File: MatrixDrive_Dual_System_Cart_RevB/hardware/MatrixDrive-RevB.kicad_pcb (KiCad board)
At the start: 2 copper layers, 100 x 65 mm, 23 parts, among them J1 MEGA_DRIVE_EDGE_VERIFY_ORIENT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, J2 USB-C, J4 CPLD JTAG, SW1 PROGRAM, SW2 MD / SMS, SW3 SMS PAUSE, U1 RP2350B QFN80, U10 STAGING SPI, U11 3V3 LDO, U13 ATF1508ASV CPLD, U14 CTRL2 XCVR, U15-U16 DATA CONTROL, U17 32KiB SMS FRAM, U2 S29GL032N TSOP48, U3 ADDR XCVR 0-7, U4 ADDR XCVR 8-15, U5 ADDR/CTRL XCVR, U6 LOW DATA BIDI, U7 HIGH DATA OUT, U9 BOOT QSPI, Y1 12MHz

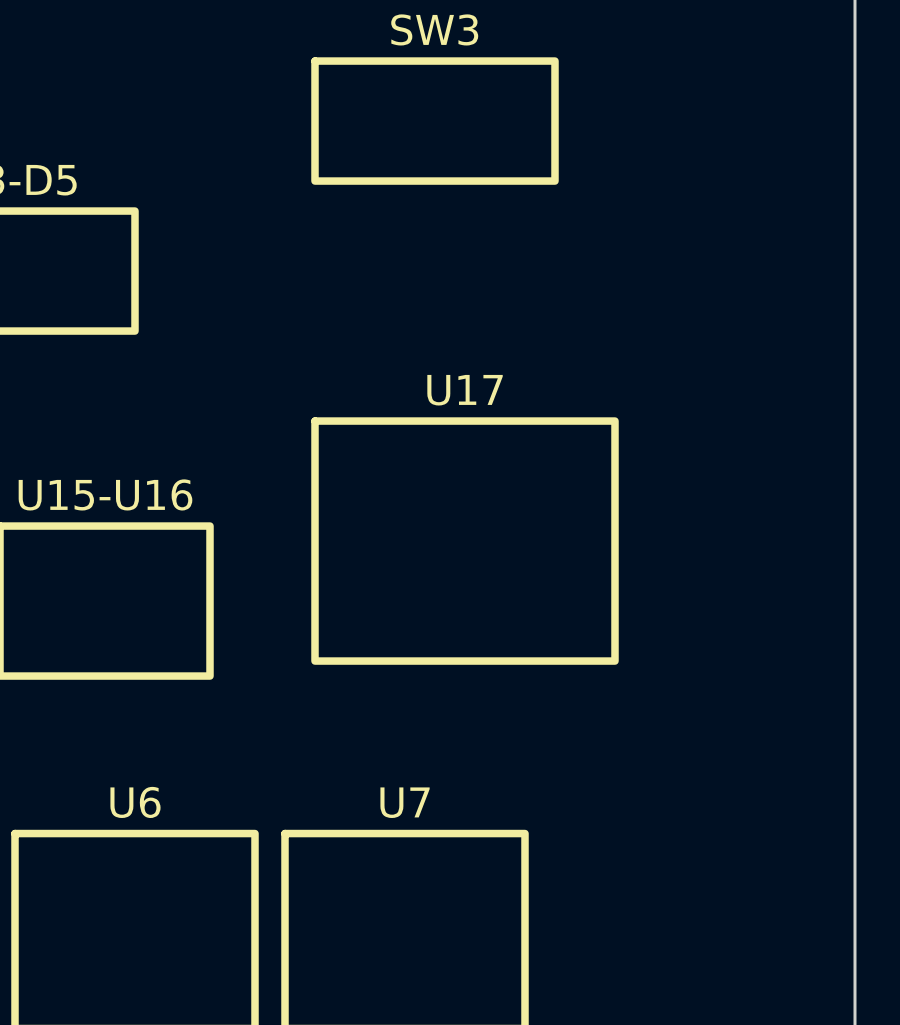
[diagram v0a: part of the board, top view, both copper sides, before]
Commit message: Add Codemasters SMS mapper and 64 KiB FRAM
Adds SW4 Sega/Codemasters selection, exact Codemasters banking and RAM decode, two-chip 64 KiB FRAM, updated hardware documentation, RTL tests, and rebuilt RP2350B firmware package.
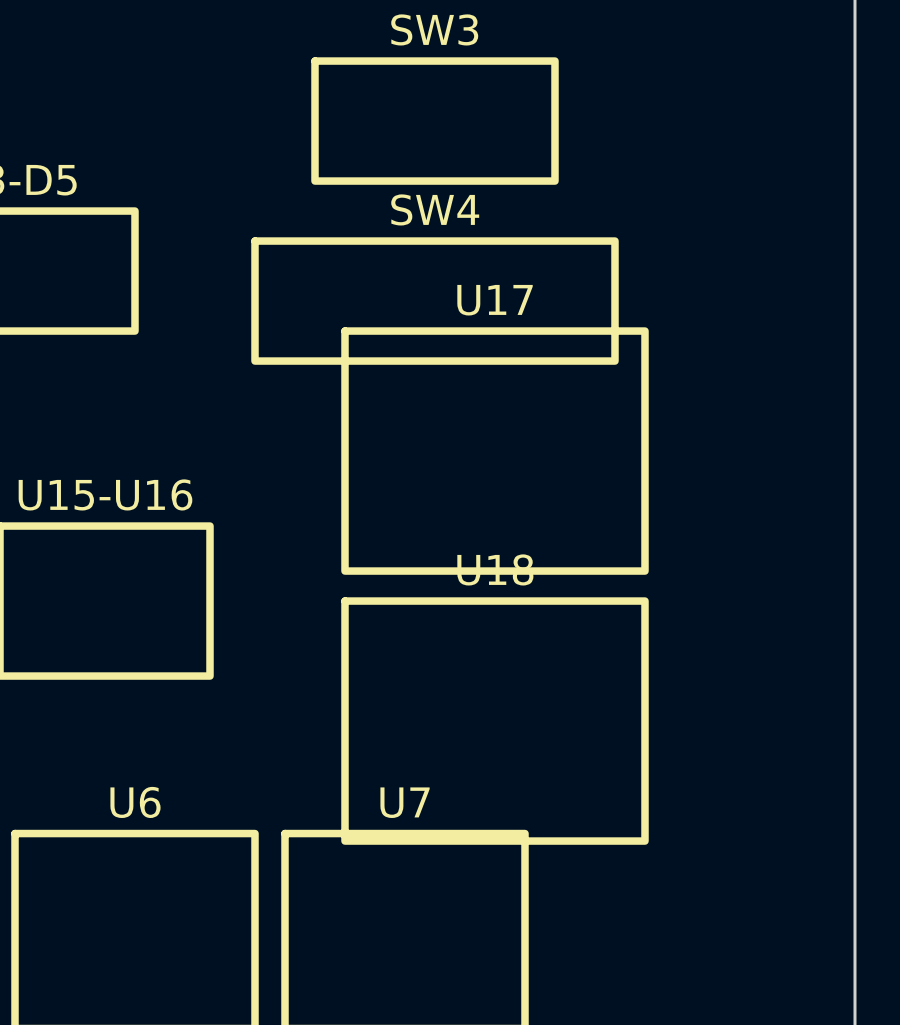
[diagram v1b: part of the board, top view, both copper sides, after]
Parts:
- added SW4: SEGA / CODEMASTERS, MatrixDrive:PLACEMENT_SW4, F.Cu at (86.0, 20.0)
- added U18: 32KiB FRAM HIGH, MatrixDrive:PLACEMENT_U18, F.Cu at (88.0, 34.0)
- U17: value 32KiB SMS FRAM -> 32KiB FRAM LOW
- moved U17 3.16 mm to (88.0, 25.0)
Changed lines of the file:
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@@
       (effects (font (size 0.8 0.8) (thickness 0.12))))
   )
-  (footprint "MatrixDrive:PLACEMENT_U17" (layer "F.Cu") (at 87.00 28.00)
+  (footprint "MatrixDrive:PLACEMENT_U17" (layer "F.Cu") (at 88.00 25.00)
     (attr board_only exclude_from_pos_files exclude_from_bom)
     (fp_rect (start -5.00 -4.00) (end 5.00 4.00)
@@
     (fp_text reference "U17" (at 0 -5.00) (layer "F.SilkS")
       (effects (font (size 1 1) (thickness 0.15))))
-    (fp_text value "32KiB SMS FRAM" (at 0 0) (layer "F.Fab")
+    (fp_text value "32KiB FRAM LOW" (at 0 0) (layer "F.Fab")
+      (effects (font (size 0.8 0.8) (thickness 0.12))))
+  )
+  (footprint "MatrixDrive:PLACEMENT_U18" (layer "F.Cu") (at 88.00 34.00)
+    (attr board_only exclude_from_pos_files exclude_from_bom)
+    (fp_rect (start -5.00 -4.00) (end 5.00 4.00)
+      (stroke (width 0.25) (type default)) (fill none) (layer "F.SilkS"))
+    (fp_text reference "U18" (at 0 -5.00) (layer "F.SilkS")
+      (effects (font (size 1 1) (thickness 0.15))))
+    (fp_text value "32KiB FRAM HIGH" (at 0 0) (layer "F.Fab")
       (effects (font (size 0.8 0.8) (thickness 0.12))))
   )
@@
       (effects (font (size 0.8 0.8) (thickness 0.12))))
   )
+  (footprint "MatrixDrive:PLACEMENT_SW4" (layer "F.Cu") (at 86.00 20.00)
+    (attr board_only exclude_from_pos_files exclude_from_bom)
+    (fp_rect (start -6.00 -2.00) (end 6.00 2.00)
+      (stroke (width 0.25) (type default)) (fill none) (layer "F.SilkS"))
+    (fp_text reference "SW4" (at 0 -3.00) (layer "F.SilkS")
+      (effects (font (size 1 1) (thickness 0.15))))
+    (fp_text value "SEGA / CODEMASTERS" (at 0 0) (layer "F.Fab")
+      (effects (font (size 0.8 0.8) (thickness 0.12))))
+  )

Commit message: Regenerate lock-on PCB template and package [skip ci]
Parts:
- added U19: MD HIGH DISABLE XCVR, MatrixDrive:PLACEMENT_U19, F.Cu at (75.0, 24.0)
- added U20: SONIC 3 SAVE FRAM, MatrixDrive:PLACEMENT_U20, F.Cu at (88.0, 51.0)
- SW4: value SEGA / CODEMASTERS -> SEGA-LINEAR / CODIES-S3 SAVE
- U15-U16: value DATA CONTROL -> DATA CONTROL ORS
- U17: value 32KiB FRAM LOW -> 32KiB SMS FRAM LOW
- U18: value 32KiB FRAM HIGH -> 32KiB SMS FRAM HIGH
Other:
- board text added: "MATRIXDRIVE REV B DUAL-SYSTEM + LOCK-ON — PLACEMENT ONLY"
- board text added: "STANDARD MD EDGE / S&K UPPER-SLOT PROFILE — VERIFY SHELL"
- board text removed: "B1/A1 AT LEFT IN THIS VIEW — VERIFY AGAINST DONOR"
- board text removed: "MATRIXDRIVE REV B DUAL-SYSTEM — PLACEMENT ONLY"
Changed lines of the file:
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@@
   (setup (pad_to_mask_clearance 0))
   (gr_rect (start 0 0) (end 100 65) (stroke (width 0.10) (type default)) (fill none) (layer "Edge.Cuts"))
-  (gr_text "MATRIXDRIVE REV B DUAL-SYSTEM — PLACEMENT ONLY" (at 50.00 3.00) (layer "F.SilkS")
+  (gr_text "MATRIXDRIVE REV B DUAL-SYSTEM + LOCK-ON — PLACEMENT ONLY" (at 50.00 3.00) (layer "F.SilkS")
     (effects (font (size 1.20 1.20) (thickness 0.20)))
   )
@@
     (fp_text reference "U15-U16" (at 0 -3.50) (layer "F.SilkS")
       (effects (font (size 1 1) (thickness 0.15))))
-    (fp_text value "DATA CONTROL" (at 0 0) (layer "F.Fab")
+    (fp_text value "DATA CONTROL ORS" (at 0 0) (layer "F.Fab")
       (effects (font (size 0.8 0.8) (thickness 0.12))))
   )
@@
     (fp_text reference "U17" (at 0 -5.00) (layer "F.SilkS")
       (effects (font (size 1 1) (thickness 0.15))))
-    (fp_text value "32KiB FRAM LOW" (at 0 0) (layer "F.Fab")
+    (fp_text value "32KiB SMS FRAM LOW" (at 0 0) (layer "F.Fab")
       (effects (font (size 0.8 0.8) (thickness 0.12))))
   )
@@
     (fp_text reference "U18" (at 0 -5.00) (layer "F.SilkS")
       (effects (font (size 1 1) (thickness 0.15))))
-    (fp_text value "32KiB FRAM HIGH" (at 0 0) (layer "F.Fab")
+    (fp_text value "32KiB SMS FRAM HIGH" (at 0 0) (layer "F.Fab")
+      (effects (font (size 0.8 0.8) (thickness 0.12))))
+  )
+  (footprint "MatrixDrive:PLACEMENT_U19" (layer "F.Cu") (at 75.00 24.00)
+    (attr board_only exclude_from_pos_files exclude_from_bom)
+    (fp_rect (start -3.00 -2.00) (end 3.00 2.00)
+      (stroke (width 0.25) (type default)) (fill none) (layer "F.SilkS"))
+    (fp_text reference "U19" (at 0 -3.00) (layer "F.SilkS")
+      (effects (font (size 1 1) (thickness 0.15))))
+    (fp_text value "MD HIGH DISABLE XCVR" (at 0 0) (layer "F.Fab")
+      (effects (font (size 0.8 0.8) (thickness 0.12))))
+  )
+  (footprint "MatrixDrive:PLACEMENT_U20" (layer "F.Cu") (at 88.00 51.00)
+    (attr board_only exclude_from_pos_files exclude_from_bom)
+    (fp_rect (start -5.00 -4.00) (end 5.00 4.00)
+      (stroke (width 0.25) (type default)) (fill none) (layer "F.SilkS"))
+    (fp_text reference "U20" (at 0 -5.00) (layer "F.SilkS")
+      (effects (font (size 1 1) (thickness 0.15))))
+    (fp_text value "SONIC 3 SAVE FRAM" (at 0 0) (layer "F.Fab")
       (effects (font (size 0.8 0.8) (thickness 0.12))))
   )
@@
   (footprint "MatrixDrive:PLACEMENT_SW4" (layer "F.Cu") (at 86.00 20.00)
     (attr board_only exclude_from_pos_files exclude_from_bom)
-    (fp_rect (start -6.00 -2.00) (end 6.00 2.00)
+    (fp_rect (start -8.00 -2.00) (end 8.00 2.00)
       (stroke (width 0.25) (type default)) (fill none) (layer "F.SilkS"))
     (fp_text reference "SW4" (at 0 -3.00) (layer "F.SilkS")
       (effects (font (size 1 1) (thickness 0.15))))
-    (fp_text value "SEGA / CODEMASTERS" (at 0 0) (layer "F.Fab")
+    (fp_text value "SEGA-LINEAR / CODIES-S3 SAVE" (at 0 0) (layer "F.Fab")
       (effects (font (size 0.8 0.8) (thickness 0.12))))
   )
@@
       (effects (font (size 0.8 0.8) (thickness 0.12))))
   )
-  (gr_text "B1/A1 AT LEFT IN THIS VIEW — VERIFY AGAINST DONOR" (at 50.00 56.00) (layer "F.SilkS")
+  (gr_text "STANDARD MD EDGE / S&K UPPER-SLOT PROFILE — VERIFY SHELL" (at 50.00 56.00) (layer "F.SilkS")
     (effects (font (size 1.20 1.20) (thickness 0.20)))
   )

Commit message: Add real 32X cartridge ROM support
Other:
- board text added: "STANDARD MD / 32X EDGE / S&K UPPER-SLOT — VERIFY SHELL"
- board text removed: "STANDARD MD EDGE / S&K UPPER-SLOT PROFILE — VERIFY SHELL"
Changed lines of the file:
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@@
       (effects (font (size 0.8 0.8) (thickness 0.12))))
   )
-  (gr_text "STANDARD MD EDGE / S&K UPPER-SLOT PROFILE — VERIFY SHELL" (at 50.00 56.00) (layer "F.SilkS")
+  (gr_text "STANDARD MD / 32X EDGE / S&K UPPER-SLOT — VERIFY SHELL" (at 50.00 56.00) (layer "F.SilkS")
     (effects (font (size 1.20 1.20) (thickness 0.20)))
   )

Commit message: Add complete MatrixDrive KiCad project
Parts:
- removed D3-D5: STATUS LEDS, MatrixDrive:PLACEMENT_D3-D5
- removed U15-U16: DATA CONTROL ORS, MatrixDrive:PLACEMENT_U15-U16
- added C1: 100nF, MatrixDrive:0603, F.Cu at (58.9, 22.4)
- added C10: 100nF, MatrixDrive:0603, F.Cu at (37.4, 26.5)
- added C11: 100nF, MatrixDrive:0603, F.Cu at (41.7, 26.5)
- added C12: 100nF, MatrixDrive:0603, F.Cu at (46.0, 26.5)
- added C13: 100nF, MatrixDrive:0603, F.Cu at (50.3, 26.5)
- added C14: 100nF, MatrixDrive:0603, F.Cu at (54.6, 26.5)
- added C15: 100nF, MatrixDrive:0603, F.Cu at (58.9, 26.5)
- added C16: 100nF, MatrixDrive:0603, F.Cu at (63.2, 26.5)
- added C17: 100nF, MatrixDrive:0603, F.Cu at (67.5, 26.5)
- added C18: 100nF, MatrixDrive:0603, F.Cu at (93.3, 26.5)
- added C19: 1uF, MatrixDrive:0603, F.Cu at (3.00, 30.6)
- added C2: 100nF, MatrixDrive:0603, F.Cu at (63.2, 22.4)
- added C20: 1uF, MatrixDrive:0603, F.Cu at (7.30, 30.6)
- added C21: 1uF, MatrixDrive:0603, F.Cu at (20.2, 30.6)
- added C22: 1uF, MatrixDrive:0603, F.Cu at (33.1, 30.6)
- added C23: 10uF, MatrixDrive:0805, F.Cu at (37.4, 30.6)
- added C24: 10uF, MatrixDrive:0805, F.Cu at (41.7, 30.6)
- added C25: 15pF, MatrixDrive:0402, F.Cu at (46.0, 30.6)
- added C26: 15pF, MatrixDrive:0402, F.Cu at (50.3, 30.6)
- added C27: 4.7uF, MatrixDrive:0603, F.Cu at (54.6, 30.6)
- added C28: TBD_REF, MatrixDrive:0402, F.Cu at (58.9, 30.6)
- added C29: TBD_REF, MatrixDrive:0402, F.Cu at (63.2, 30.6)
- added C3: 100nF, MatrixDrive:0603, F.Cu at (67.5, 22.4)
- added C30: TBD_REF, MatrixDrive:0402, F.Cu at (67.5, 30.6)
- added C31: TBD_REF, MatrixDrive:0402, F.Cu at (93.3, 30.6)
- added C32: TBD_REF, MatrixDrive:0402, F.Cu at (3.00, 34.7)
- added C33: TBD_REF, MatrixDrive:0402, F.Cu at (7.30, 34.7)
- added C34: 100nF, MatrixDrive:0603, F.Cu at (20.2, 34.7)
- added C35: 100nF, MatrixDrive:0603, F.Cu at (33.1, 34.7)
- added C36: 100nF, MatrixDrive:0603, F.Cu at (37.4, 34.7)
- added C4: 100nF, MatrixDrive:0603, F.Cu at (80.4, 22.4)
- added C5: 100nF, MatrixDrive:0603, F.Cu at (93.3, 22.4)
- added C6: 100nF, MatrixDrive:0603, F.Cu at (3.00, 26.5)
- added C7: 100nF, MatrixDrive:0603, F.Cu at (7.30, 26.5)
- added C8: 100nF, MatrixDrive:0603, F.Cu at (20.2, 26.5)
- added C9: 100nF, MatrixDrive:0603, F.Cu at (33.1, 26.5)
- added D1: PMEG2010AEB, MatrixDrive:SOD_523, F.Cu at (15.9, 6.00)
- added D2: PMEG2010AEB, MatrixDrive:SOD_523, F.Cu at (28.8, 6.00)
- added D3: GREEN_LED, MatrixDrive:0603_LED, F.Cu at (33.1, 6.00)
- added D4: AMBER_LED, MatrixDrive:0603_LED, F.Cu at (37.4, 6.00)
- added D5: RED_LED, MatrixDrive:0603_LED, F.Cu at (41.7, 6.00)
- added F1: MF-MSMF020-2, MatrixDrive:1812, F.Cu at (3.00, 6.00)
- added J3: SWD_UART_2x5 DNP, MatrixDrive:HDR_2x5_1_27, F.Cu at (66.0, 5.00)
- added Q1: 2N7002, MatrixDrive:SOT_23, F.Cu at (80.4, 6.00)
- added Q2: 2N7002, MatrixDrive:SOT_23, F.Cu at (93.3, 6.00)
- added Q3: 2N7002, MatrixDrive:SOT_23, F.Cu at (3.00, 10.1)
- added Q4: 2N7002, MatrixDrive:SOT_23, F.Cu at (7.30, 10.1)
- added R1: 5.1k, MatrixDrive:0603, F.Cu at (33.1, 10.1)
- added R10: 1k, MatrixDrive:0603, F.Cu at (15.9, 14.2)
- added R11: 1k, MatrixDrive:0603, F.Cu at (20.2, 14.2)
- added R12: 10k, MatrixDrive:0603, F.Cu at (24.5, 14.2)
- added R13: 0R, MatrixDrive:0603, F.Cu at (28.8, 14.2)
- added R14: 100k, MatrixDrive:0603, F.Cu at (33.1, 14.2)
- added R15: 10k DNP, MatrixDrive:0603, F.Cu at (54.6, 14.2)
- added R16: 10k DNP, MatrixDrive:0603, F.Cu at (67.5, 14.2)
- added R17: 10k DNP, MatrixDrive:0603, F.Cu at (71.8, 14.2)
- added R18: 10k DNP, MatrixDrive:0603, F.Cu at (76.1, 14.2)
- added R19: 10k, MatrixDrive:0603, F.Cu at (80.4, 14.2)
- added R2: 5.1k, MatrixDrive:0603, F.Cu at (67.5, 10.1)
- added R20: 10k, MatrixDrive:0603, F.Cu at (93.3, 14.2)
- added R21: 10k, MatrixDrive:0603, F.Cu at (3.00, 18.3)
- added R22: 10k, MatrixDrive:0603, F.Cu at (7.30, 18.3)
- added R23: 10k, MatrixDrive:0603, F.Cu at (11.6, 18.3)
- added R24: 33R, MatrixDrive:0603, F.Cu at (15.9, 18.3)
- added R25: 10k, MatrixDrive:0603, F.Cu at (20.2, 18.3)
- added R26: 10k, MatrixDrive:0603, F.Cu at (33.1, 18.3)
- added R27: 10k, MatrixDrive:0603, F.Cu at (37.4, 18.3)
- added R28: 1k, MatrixDrive:0603, F.Cu at (41.7, 18.3)
- added R29: 100k, MatrixDrive:0603, F.Cu at (54.6, 18.3)
- added R3: 27R, MatrixDrive:0603, F.Cu at (71.8, 10.1)
- added R30: 100k, MatrixDrive:0603, F.Cu at (58.9, 18.3)
- added R31: 10k, MatrixDrive:0603, F.Cu at (63.2, 18.3)
- added R32: 10k, MatrixDrive:0603, F.Cu at (67.5, 18.3)
- added R33: 10k, MatrixDrive:0603, F.Cu at (71.8, 18.3)
- added R34: 10k, MatrixDrive:0603, F.Cu at (76.1, 18.3)
- added R35: 10k, MatrixDrive:0603, F.Cu at (80.4, 18.3)
- added R36: 10k, MatrixDrive:0603, F.Cu at (93.3, 18.3)
- added R37: 100k, MatrixDrive:0603, F.Cu at (3.00, 22.4)
- added R38: 100k, MatrixDrive:0603, F.Cu at (7.30, 22.4)
- added R39: 100k, MatrixDrive:0603, F.Cu at (11.6, 22.4)
- added R4: 27R, MatrixDrive:0603, F.Cu at (76.1, 10.1)
- added R40: 100k, MatrixDrive:0603, F.Cu at (15.9, 22.4)
- added R41: 100k, MatrixDrive:0603, F.Cu at (20.2, 22.4)
- added R42: 10k, MatrixDrive:0603, F.Cu at (33.1, 22.4)
- added R43: 10k, MatrixDrive:0603, F.Cu at (37.4, 22.4)
- added R44: 100k, MatrixDrive:0603, F.Cu at (41.7, 22.4)
- added R45: 10k, MatrixDrive:0603, F.Cu at (54.6, 22.4)
- added R5: 10k, MatrixDrive:0603, F.Cu at (80.4, 10.1)
- added R6: 100k, MatrixDrive:0603, F.Cu at (93.3, 10.1)
- added R7: 100k, MatrixDrive:0603, F.Cu at (3.00, 14.2)
- added R8: 100k, MatrixDrive:0603, F.Cu at (7.30, 14.2)
- added R9: 1k, MatrixDrive:0603, F.Cu at (11.6, 14.2)
- added TP1: CART_5V, MatrixDrive:TP_SMD_1MM, F.Cu at (41.7, 34.7)
- added TP10: ROM_CE_N, MatrixDrive:TP_SMD_1MM, F.Cu at (80.4, 34.7)
- added TP11: ROM_OE_N, MatrixDrive:TP_SMD_1MM, F.Cu at (93.3, 34.7)
- added TP12: ROM_WE_N, MatrixDrive:TP_SMD_1MM, F.Cu at (3.00, 38.8)
- added TP13: FRAM_CE_N, MatrixDrive:TP_SMD_1MM, F.Cu at (7.30, 38.8)
- added TP14: FRAM_HI_CE_N, MatrixDrive:TP_SMD_1MM, F.Cu at (41.7, 38.8)
- added TP15: FRAM_OE_N, MatrixDrive:TP_SMD_1MM, F.Cu at (46.0, 38.8)
- added TP16: FRAM_WE_N, MatrixDrive:TP_SMD_1MM, F.Cu at (50.3, 38.8)
- added TP17: MD_FRAM_CE_N, MatrixDrive:TP_SMD_1MM, F.Cu at (63.2, 38.8)
- added TP18: MD_HIGH_DISABLE_3V3, MatrixDrive:TP_SMD_1MM, F.Cu at (67.5, 38.8)
- added TP19: LWR_3V3, MatrixDrive:TP_SMD_1MM, F.Cu at (93.3, 38.8)
- added TP2: USB_VBUS, MatrixDrive:TP_SMD_1MM, F.Cu at (46.0, 34.7)
- added TP20: UWR_3V3, MatrixDrive:TP_SMD_1MM, F.Cu at (3.00, 42.9)
- added TP21: AS_3V3, MatrixDrive:TP_SMD_1MM, F.Cu at (7.30, 42.9)
- added TP22: TIME_3V3, MatrixDrive:TP_SMD_1MM, F.Cu at (41.7, 42.9)
- added TP3: SYS_5V, MatrixDrive:TP_SMD_1MM, F.Cu at (50.3, 34.7)
- added TP4: 3V3, MatrixDrive:TP_SMD_1MM, F.Cu at (54.6, 34.7)
- added TP5: GND, MatrixDrive:TP_SMD_1MM, F.Cu at (58.9, 34.7)
- added TP6: BUS_DISABLE, MatrixDrive:TP_SMD_1MM, F.Cu at (63.2, 34.7)
- added TP7: SMS_MODE_3V3, MatrixDrive:TP_SMD_1MM, F.Cu at (67.5, 34.7)
- added TP8: SMS_MODE_5V, MatrixDrive:TP_SMD_1MM, F.Cu at (71.8, 34.7)
- added TP9: USB_MODE_3V3, MatrixDrive:TP_SMD_1MM, F.Cu at (76.1, 34.7)
- added U12: TPD2EUSB30DRTR, MatrixDrive:DRT_9_LOGICAL, F.Cu at (55.0, 7.00)
- added U15: SN74LVC2G32DCUR, MatrixDrive:VSSOP_8, F.Cu at (73.0, 30.0)
- added U16: SN74LVC1G04DBVR, MatrixDrive:SOT_23_5, F.Cu at (78.0, 30.0)
- added U8: SN74LVC1G17DBVR, MatrixDrive:SOT_23_5, F.Cu at (22.0, 9.00)
- J1: value MEGA_DRIVE_EDGE_VERIFY_ORIENTATION -> MEGA_DRIVE_EDGE
- J2: value USB-C -> USB4105-GF-A; footprint MatrixDrive:PLACEMENT_J2 -> MatrixDrive:USB_C_16P
- J4: value CPLD JTAG -> CPLD_JTAG_2x5; footprint MatrixDrive:PLACEMENT_J4 -> MatrixDrive:HDR_2x5_1_27
- L1: value POLARISED 3V3 CORE L -> 3.3uH; footprint MatrixDrive:PLACEMENT_L1 -> MatrixDrive:2016
- SW1: footprint MatrixDrive:PLACEMENT_SW1 -> MatrixDrive:SW_2P
- SW2: value MD / SMS -> MD_SMS_DPDT; footprint MatrixDrive:PLACEMENT_SW2 -> MatrixDrive:SW_DPDT_6P
- SW3: value SMS PAUSE -> SMS_PAUSE; footprint MatrixDrive:PLACEMENT_SW3 -> MatrixDrive:SW_2P
- SW4: value SEGA-LINEAR / CODIES-S3 SAVE -> PROFILE_SPDT; footprint MatrixDrive:PLACEMENT_SW4 -> MatrixDrive:SW_SPDT_3P
- U1: value RP2350B QFN80 -> RP2350B; footprint MatrixDrive:PLACEMENT_U1 -> MatrixDrive:UNVERIFIED_LOGICAL_PACKAGE
- U10: value STAGING SPI -> W25Q128JVSIQ; footprint MatrixDrive:PLACEMENT_U10 -> MatrixDrive:SOIC_8
- U11: value 3V3 LDO -> TLV75533PDBVR; footprint MatrixDrive:PLACEMENT_U11 -> MatrixDrive:SOT_23_5
- U13: value ATF1508ASV CPLD -> ATF1508ASV-15AU100; footprint MatrixDrive:PLACEMENT_U13 -> MatrixDrive:TQFP_100_UNASSIGNED
- U14: value CTRL2 XCVR -> SN74LVC8T245PWR; footprint MatrixDrive:PLACEMENT_U14 -> MatrixDrive:TSSOP_24_LOGICAL
- U17: value 32KiB SMS FRAM LOW -> FM18W08-SG; footprint MatrixDrive:PLACEMENT_U17 -> MatrixDrive:SOIC_28_LOGICAL
- U18: value 32KiB SMS FRAM HIGH -> FM18W08-SG; footprint MatrixDrive:PLACEMENT_U18 -> MatrixDrive:SOIC_28_LOGICAL
- U19: value MD HIGH DISABLE XCVR -> SN74LVC1T45DBVR; footprint MatrixDrive:PLACEMENT_U19 -> MatrixDrive:SOT_23_6
- U2: value S29GL032N TSOP48 -> S29GL032N90TFI040; footprint MatrixDrive:PLACEMENT_U2 -> MatrixDrive:TSOP_I_48_UNVERIFIED_PINMAP
- U20: value SONIC 3 SAVE FRAM -> FM18W08-SG; footprint MatrixDrive:PLACEMENT_U20 -> MatrixDrive:SOIC_28_LOGICAL
- U3: value ADDR XCVR 0-7 -> SN74LVC8T245PWR; footprint MatrixDrive:PLACEMENT_U3 -> MatrixDrive:TSSOP_24_LOGICAL
- U4: value ADDR XCVR 8-15 -> SN74LVC8T245PWR; footprint MatrixDrive:PLACEMENT_U4 -> MatrixDrive:TSSOP_24_LOGICAL
- U5: value ADDR/CTRL XCVR -> SN74LVC8T245PWR; footprint MatrixDrive:PLACEMENT_U5 -> MatrixDrive:TSSOP_24_LOGICAL
- U6: value LOW DATA BIDI -> SN74LVC8T245PWR; footprint MatrixDrive:PLACEMENT_U6 -> MatrixDrive:TSSOP_24_LOGICAL
- U7: value HIGH DATA OUT -> SN74LVC8T245PWR; footprint MatrixDrive:PLACEMENT_U7 -> MatrixDrive:TSSOP_24_LOGICAL
- U9: value BOOT QSPI -> W25Q16JVSSIQ; footprint MatrixDrive:PLACEMENT_U9 -> MatrixDrive:SOIC_8
- Y1: value 12MHz -> 12MHz_CRYSTAL; footprint MatrixDrive:PLACEMENT_Y1 -> MatrixDrive:3225_4P
- moved SW1 44.3 mm to (28.8, 10.1)
- moved Y1 31.8 mm to (71.8, 6.00)
- moved L1 19.1 mm to (76.1, 6.00)
- moved U10 3.16 mm to (62.0, 13.0)
- moved U14 3.00 mm to (13.0, 30.0)
- moved U18 2.00 mm to (88.0, 36.0)
- moved J2 1.41 mm to (50.0, 2.50)
- moved U1 1.41 mm to (49.0, 15.0)
- moved U7 1.41 mm to (86.0, 42.0)
- moved U9 1.41 mm to (38.0, 13.0)
- moved J4 1.00 mm to (8.00, 5.00)
- moved U11 1.00 mm to (13.0, 10.0)
- moved U13 1.00 mm to (28.0, 26.0)
- moved U17 1.00 mm to (88.0, 24.0)
- moved U2 1.00 mm to (55.0, 45.0)
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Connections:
- J1 pad A1: (no net) -> GND
- J1 pad A10: (no net) -> VA14
- J1 pad A11: (no net) -> VA4
- J1 pad A12: (no net) -> VA15
- J1 pad A13: (no net) -> VA3
- J1 pad A14: (no net) -> VA16
- J1 pad A15: (no net) -> VA2
- J1 pad A16: (no net) -> VA17
- J1 pad A17: (no net) -> VA1
- J1 pad A18: (no net) -> GND
- J1 pad A19: (no net) -> VD7
- J1 pad A2: (no net) -> CART_5V_IN
- J1 pad A20: (no net) -> VD0
- J1 pad A21: (no net) -> VD8
- J1 pad A22: (no net) -> VD6
- J1 pad A23: (no net) -> VD1
- J1 pad A24: (no net) -> VD9
- J1 pad A25: (no net) -> VD5
- J1 pad A26: (no net) -> VD2
- J1 pad A27: (no net) -> VD10
- J1 pad A28: (no net) -> VD4
- J1 pad A29: (no net) -> VD3
- J1 pad A3: (no net) -> VA8
- J1 pad A30: (no net) -> VD11
- J1 pad A31: (no net) -> CART_5V_IN
- J1 pad A32: (no net) -> GND
- J1 pad A4: (no net) -> VA11
- J1 pad A5: (no net) -> VA7
- J1 pad A6: (no net) -> VA12
- J1 pad A7: (no net) -> VA6
- J1 pad A8: (no net) -> VA13
- J1 pad A9: (no net) -> VA5
- J1 pad B10: (no net) -> VA22
- J1 pad B11: (no net) -> VA23_PAUSE
- J1 pad B16: (no net) -> CAS0_N
- J1 pad B17: (no net) -> CE0_N
- J1 pad B18: (no net) -> AS_N
- J1 pad B19: (no net) -> VCLK
- J1 pad B2: (no net) -> MRES_N
- J1 pad B21: (no net) -> CAS2_N
- J1 pad B22: (no net) -> VD15
- J1 pad B23: (no net) -> VD14
- J1 pad B24: (no net) -> VD13
- J1 pad B25: (no net) -> VD12
- J1 pad B27: (no net) -> VRES_N
- J1 pad B28: (no net) -> LWR_N
- J1 pad B29: (no net) -> UWR_N
- J1 pad B30: (no net) -> M3_N
- J1 pad B31: (no net) -> TIME_N
- J1 pad B32: (no net) -> CART_N
- J1 pad B4: (no net) -> VA9
- J1 pad B5: (no net) -> VA10
- J1 pad B6: (no net) -> VA18
- J1 pad B7: (no net) -> VA19
- J1 pad B8: (no net) -> VA20
- J1 pad B9: (no net) -> VA21
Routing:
- added copper zone on B.Cu, net GND
- added copper zone on F.Cu, net GND
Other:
- board text added: "DO NOT FABRICATE - UNROUTED / PROGRAMMABLE PIN MAPS UNVERIFIED"
- board text added: "MATRIXDRIVE REV B - NETLISTED ENGINEERING PCB"
- board text removed: "DO NOT FABRICATE UNTIL SCHEMATIC/DRC REVIEW"
- board text removed: "MATRIXDRIVE REV B DUAL-SYSTEM + LOCK-ON — PLACEMENT ONLY"
- board text removed: "STANDARD MD / 32X EDGE / S&K UPPER-SLOT — VERIFY SHELL"

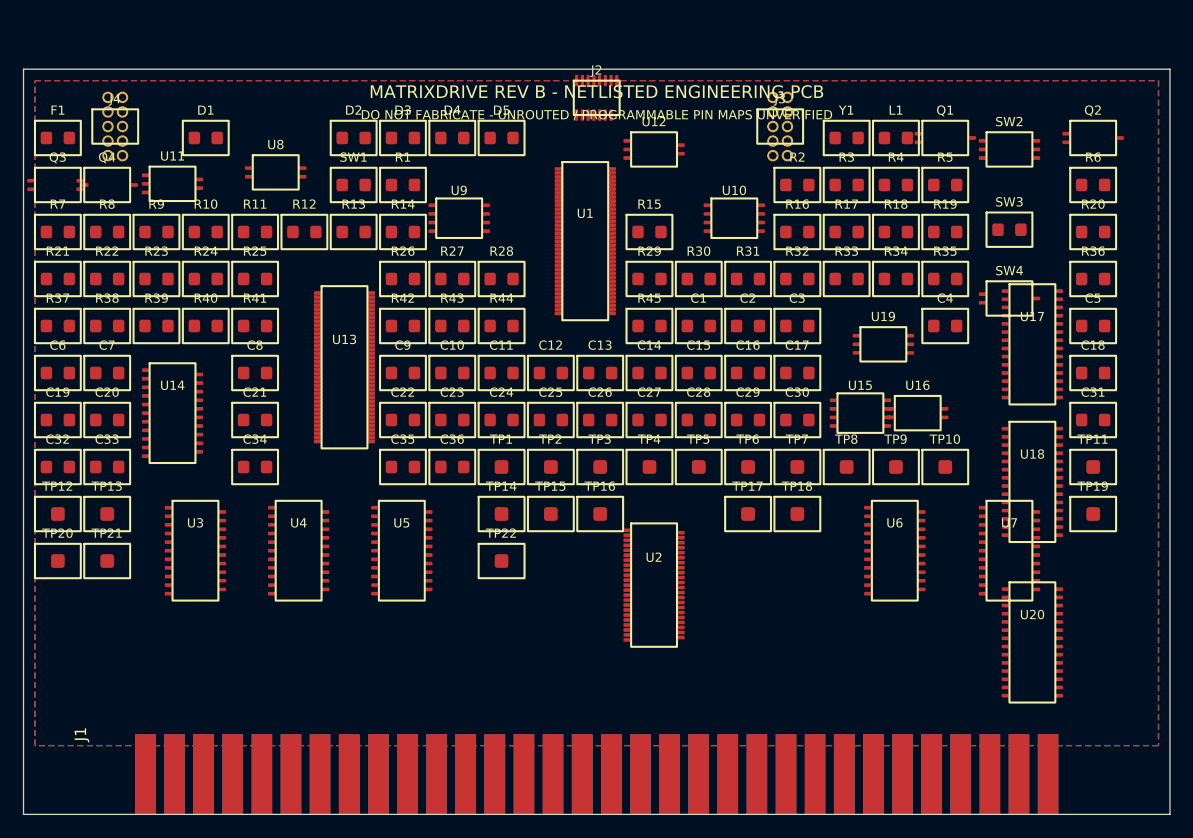
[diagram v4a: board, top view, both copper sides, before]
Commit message: Route MatrixDrive PCB for KiCad DRC
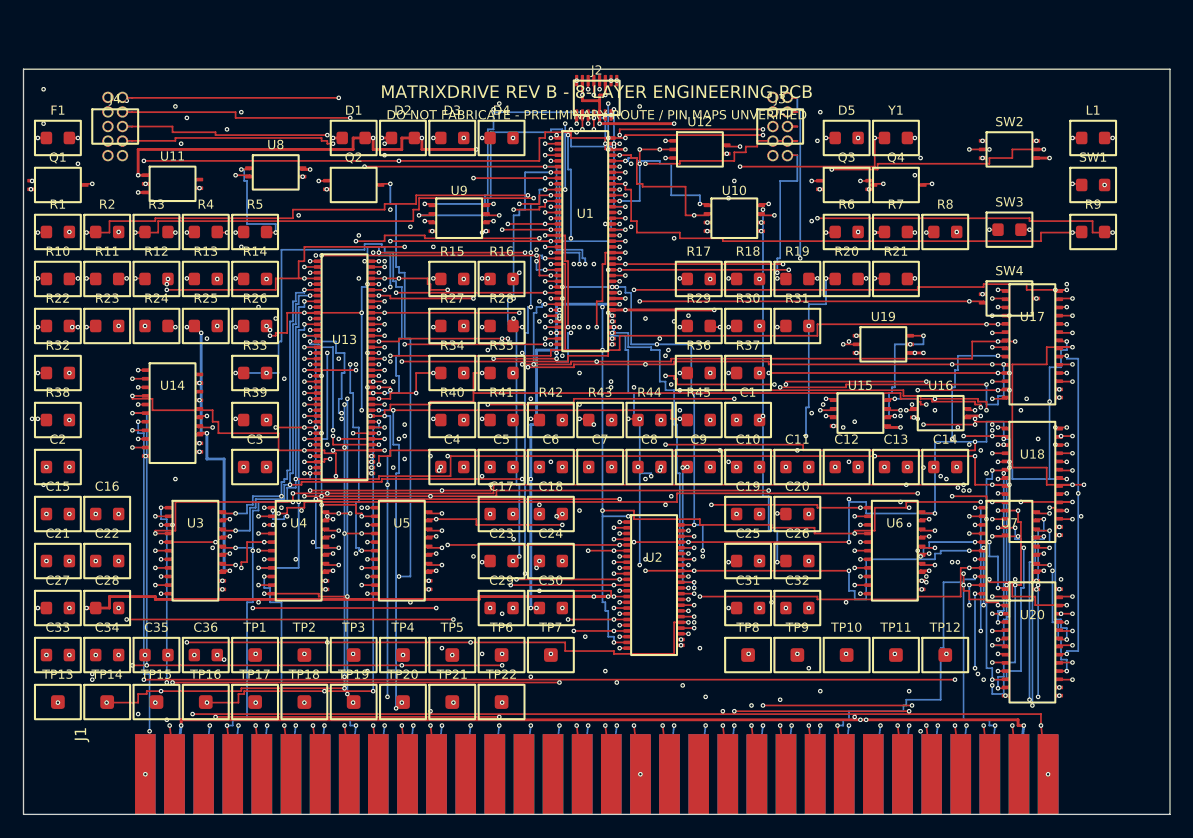
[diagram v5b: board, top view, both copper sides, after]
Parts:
- moved R9 81.7 mm to (93.3, 14.2)
- moved TP12 78.4 mm to (80.4, 51.1)
- moved Q1 77.5 mm to (3.00, 10.1)
- moved R8 73.1 mm to (80.4, 14.2)
- moved R21 73.1 mm to (76.1, 18.3)
- moved R7 73.1 mm to (76.1, 14.2)
- moved Q3 68.8 mm to (71.8, 10.1)
- moved Q4 68.8 mm to (76.1, 10.1)
- moved TP19 66.6 mm to (28.8, 55.2)
- moved C32 65.7 mm to (67.5, 47.0)
- moved R32 65.0 mm to (3.00, 26.5)
- moved Q2 64.6 mm to (28.8, 10.1)
- moved SW1 64.5 mm to (93.3, 10.1)
- moved C2 61.4 mm to (3.00, 34.7)
- moved C19 60.8 mm to (63.2, 38.8)
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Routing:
- net CART_5V: track 0.00 -> 259.7 mm, vias 0 -> 26
- net SMS_MODE_3V3: track 0.00 -> 196.8 mm, vias 0 -> 15
- net BUS_DISABLE: track 0.00 -> 195.4 mm, vias 0 -> 20
- net MEM_D1: track 0.00 -> 166.2 mm, vias 0 -> 15
- net MEM_D0: track 0.00 -> 160.8 mm, vias 0 -> 16
- net MEM_D6: track 0.00 -> 160.6 mm, vias 0 -> 14
- net MEM_D5: track 0.00 -> 158.6 mm, vias 0 -> 13
- net MEM_D7: track 0.00 -> 154.3 mm, vias 0 -> 13
- net MEM_D4: track 0.00 -> 153.5 mm, vias 0 -> 10
- net CART_A4: track 0.00 -> 151.0 mm, vias 0 -> 10
- net CART_A3: track 0.00 -> 151.0 mm, vias 0 -> 13
- net MEM_D2: track 0.00 -> 148.9 mm, vias 0 -> 12
- net CART_5V_IN: track 0.00 -> 147.7 mm, vias 0 -> 4
- net MEM_D3: track 0.00 -> 146.2 mm, vias 0 -> 11
- net FRAM_OE_N: track 0.00 -> 145.8 mm, vias 0 -> 11
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- added copper zone on In6.Cu, net 3V3
- added copper zone on In1.Cu, net GND
- removed copper zone on B.Cu, net GND
- removed copper zone on F.Cu, net GND
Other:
- copper layers 2 -> 8
- board text added: "DO NOT FABRICATE - PRELIMINARY ROUTE / PIN MAPS UNVERIFIED"
- board text added: "MATRIXDRIVE REV B - 8-LAYER ENGINEERING PCB"
- board text removed: "DO NOT FABRICATE - UNROUTED / PROGRAMMABLE PIN MAPS UNVERIFIED"
- board text removed: "MATRIXDRIVE REV B - NETLISTED ENGINEERING PCB"
